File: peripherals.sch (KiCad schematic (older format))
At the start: 31 parts, among them J1 Conn_SWD, M1 Vibrator, Q1 NTR5103N, SW1 Btn_Up, SW2 Btn_Down, SW3 Btn_Select, SW4 Btn_Back, U1 ATSAMD21J18A-MU

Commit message: Finish up the schematic
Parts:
- removed C1, C3, C4, C5: 0.1uF, Capacitor_SMD:C_0603_1608Metric, symbol Device:C_Small
- removed C2: 4.7uF, Capacitor_SMD:C_0603_1608Metric, symbol Device:C_Small
- removed C6: 1uF, Capacitor_SMD:C_0603_1608Metric, symbol Device:C_Small
- removed D1: LED_TopLeft, LED_SMD_Extra:LED_RGBA_0606, symbol Device_Extra:LED_RGBA
- removed D2: LED_TopRight, LED_SMD_Extra:LED_RGBA_0606, symbol Device_Extra:LED_RGBA
- removed D3: LED_BottomLeft, LED_SMD_Extra:LED_RGBA_0606, symbol Device_Extra:LED_RGBA
- removed D4: LED_BottomRight, LED_SMD_Extra:LED_RGBA_0606, symbol Device_Extra:LED_RGBA
- removed J1: Conn_SWD, Connector_JST:JST_SH_SM04B-SRSS-TB_1x04-1MP_P1.00mm_Horizontal, symbol Connector_Generic:Conn_01x04
- removed M1: Vibrator, Buzzer_Beeper_Extra:C1026B, symbol Motor:Motor_DC
- removed Q1: NTR5103N, Package_TO_SOT_SMD:SOT-23, symbol Transistor_FET:BSS138
- removed R1: 1K, Resistor_SMD:R_0603_1608Metric, symbol Device:R_Small
- removed R10, R11, R12, R13, R2, R3, R4, R5, R6, R7, R8, R9: 360R, Resistor_SMD:R_0603_1608Metric, symbol Device:R_Small
- removed SW1: Btn_Up, Button_Switch_SMD_Extra:KLS7-TS2402, symbol Switch:SW_Push
- removed SW2: Btn_Down, Button_Switch_SMD_Extra:KLS7-TS2402, symbol Switch:SW_Push
- removed SW3: Btn_Select, Button_Switch_SMD_Extra:KLS7-TS2402, symbol Switch:SW_Push
- removed SW4: Btn_Back, Button_Switch_SMD_Extra:KLS7-TS2402, symbol Switch:SW_Push
- removed U1: ATSAMD21J18A-MU, Package_DFN_QFN:QFN-64-1EP_9x9mm_P0.5mm_EP4.7x4.7mm, symbol MCU_Microchip_SAMD:ATSAMD21J18A-MU
- added ANT1: ACAG1204-433-T, RF_Antenna_Extra:ACAG1204, symbol Device:Antenna
- added C10, C11, C12, C13, C14, C15, C9: 0.1uF, Capacitor_SMD:C_0603_1608Metric, symbol Device:C_Small
- added LS1: Speaker, symbol Device:Speaker
- added MK1: SPH0641LM4H, Sensor_Audio_Extra:SPH0641LM4H, symbol Sensor_Audio_Extra:SPH0641LM4H
- added R14, R15: 10K, Resistor_SMD:R_0603_1608Metric, symbol Device:R_Small
- added R16: 17K, Resistor_SMD:R_0603_1608Metric, symbol Device:R_Small
- added U3: LIS3DH, Package_LGA:LGA-16_3x3mm_P0.5mm_LayoutBorder3x5y, symbol Sensor_Motion_Extra:LIS3DH
- added U4: LPH7366, Display_Extra:Nokia_5110-3310_LCD, symbol Display_Graphic_Extra:LPH7366
- added U5: 26VF0168IS2AE, Package_SO:SOIJ-8_5.3x5.3mm_P1.27mm, symbol Memory_Flash_Extra:26VF0168IS2AE
- added U6: RFM69HCW, RF_Module:HOPERF_RFM69HW, symbol RF_AM_FM_Extra:RFM69HCW
- added U7: PAM8301, Package_TO_SOT_SMD:SOT-23-6, symbol Amplifier_Audio_Extra:PAM8301
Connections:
- net labels removed: +1V2, BTN_BACK, BTN_DOWN, BTN_SELECT, BTN_UP, LED1_B, LED1_G, LED1_R, LED2_B, LED2_G, LED2_R, LED3_B, LED3_G, LED3_R, LED4_B, LED4_G, LED4_R, SWDCLK, SWDIO, USB_D+, USB_D-, VIBRATOR
- wire segments 154 -> 93
- no-connect marks 1 -> 7
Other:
- note added: "433MHz Transceiver"
- note added: "Accelerometer"
- note added: "Display"
- note added: "Microphone"
- note added: "SPI Flash"
- note added: "Speaker"
- note removed: "I2SD1"
- note removed: "I2SSCK"
- note removed: "SERCOM0 - Display\nSERCOM1 - Accelerometer\nSERCOM3 - Flash\nSERCOM4 - RFM"
- note removed: "SERCOM0.0"
- note removed: "SERCOM0.1"
- note removed: "SERCOM1.0"
- note removed: "SERCOM1.1"
- note removed: "SERCOM3.0"
- note removed: "SERCOM3.2\n"
- note removed: "SERCOM3.3"
- note removed: "SERCOM4.0\n"
- note removed: "SERCOM4.1"
- note removed: "SERCOM4.2"
- note removed: "TCC"
- note removed: "VOUT0"

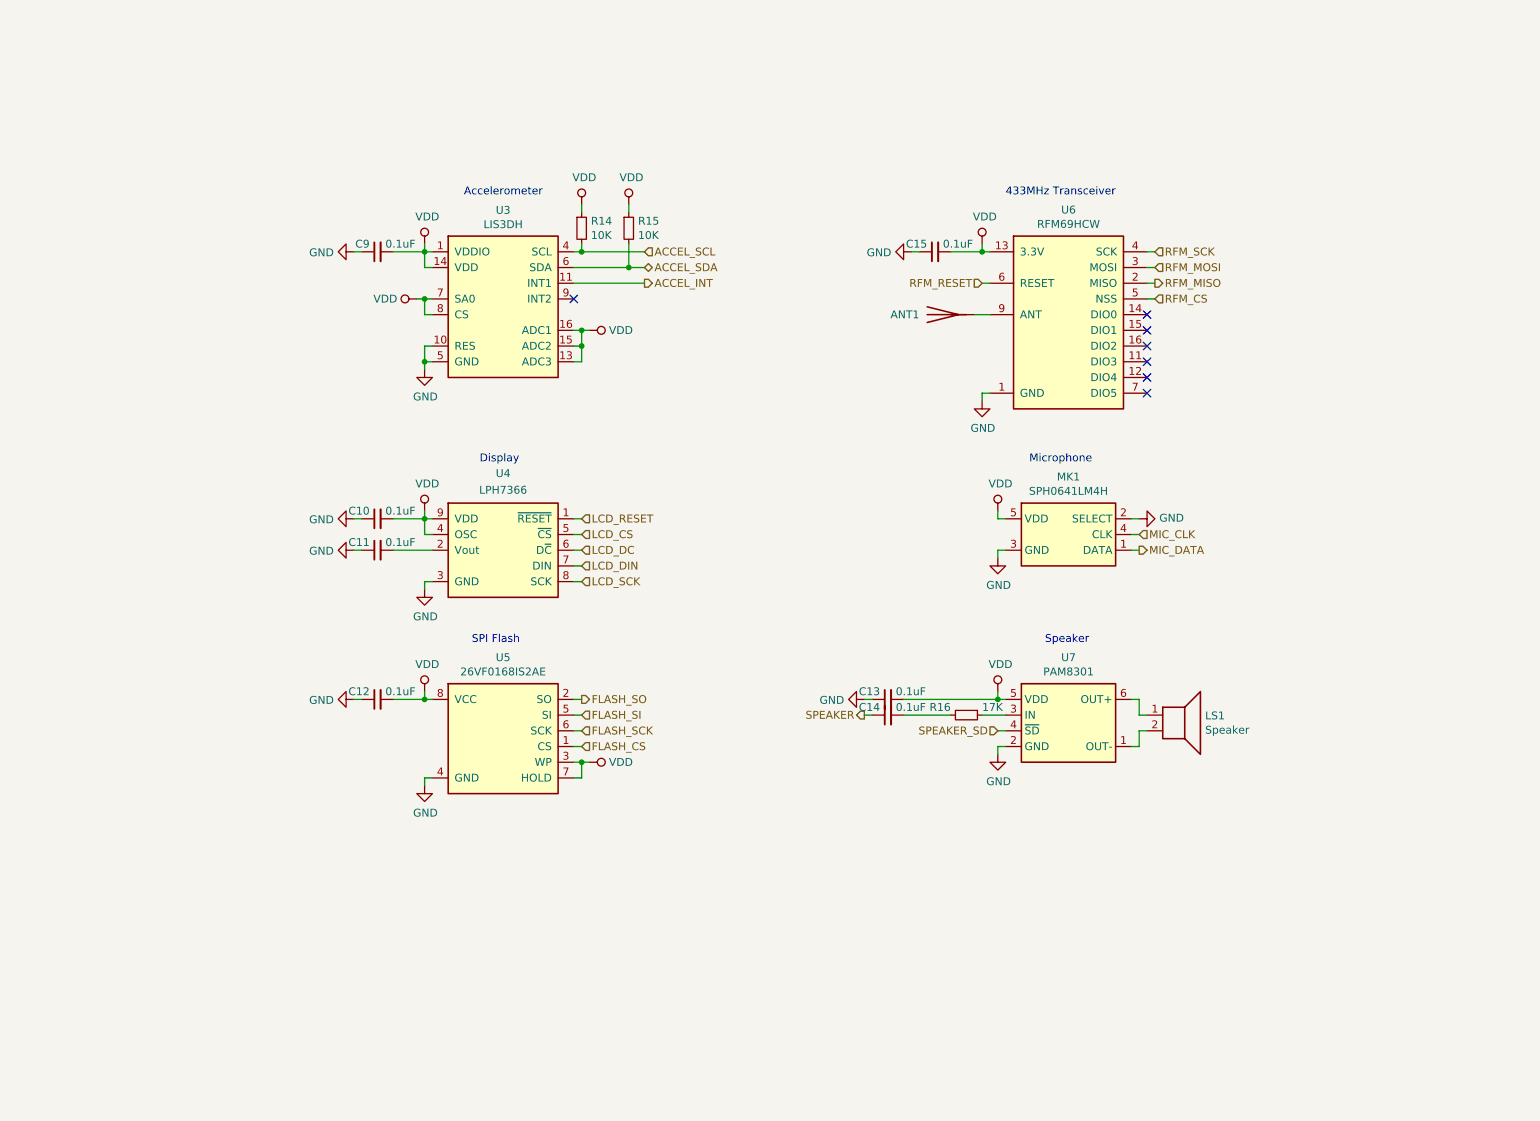
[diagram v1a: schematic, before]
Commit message: Change of plans, now a nRF52840 with E-ink
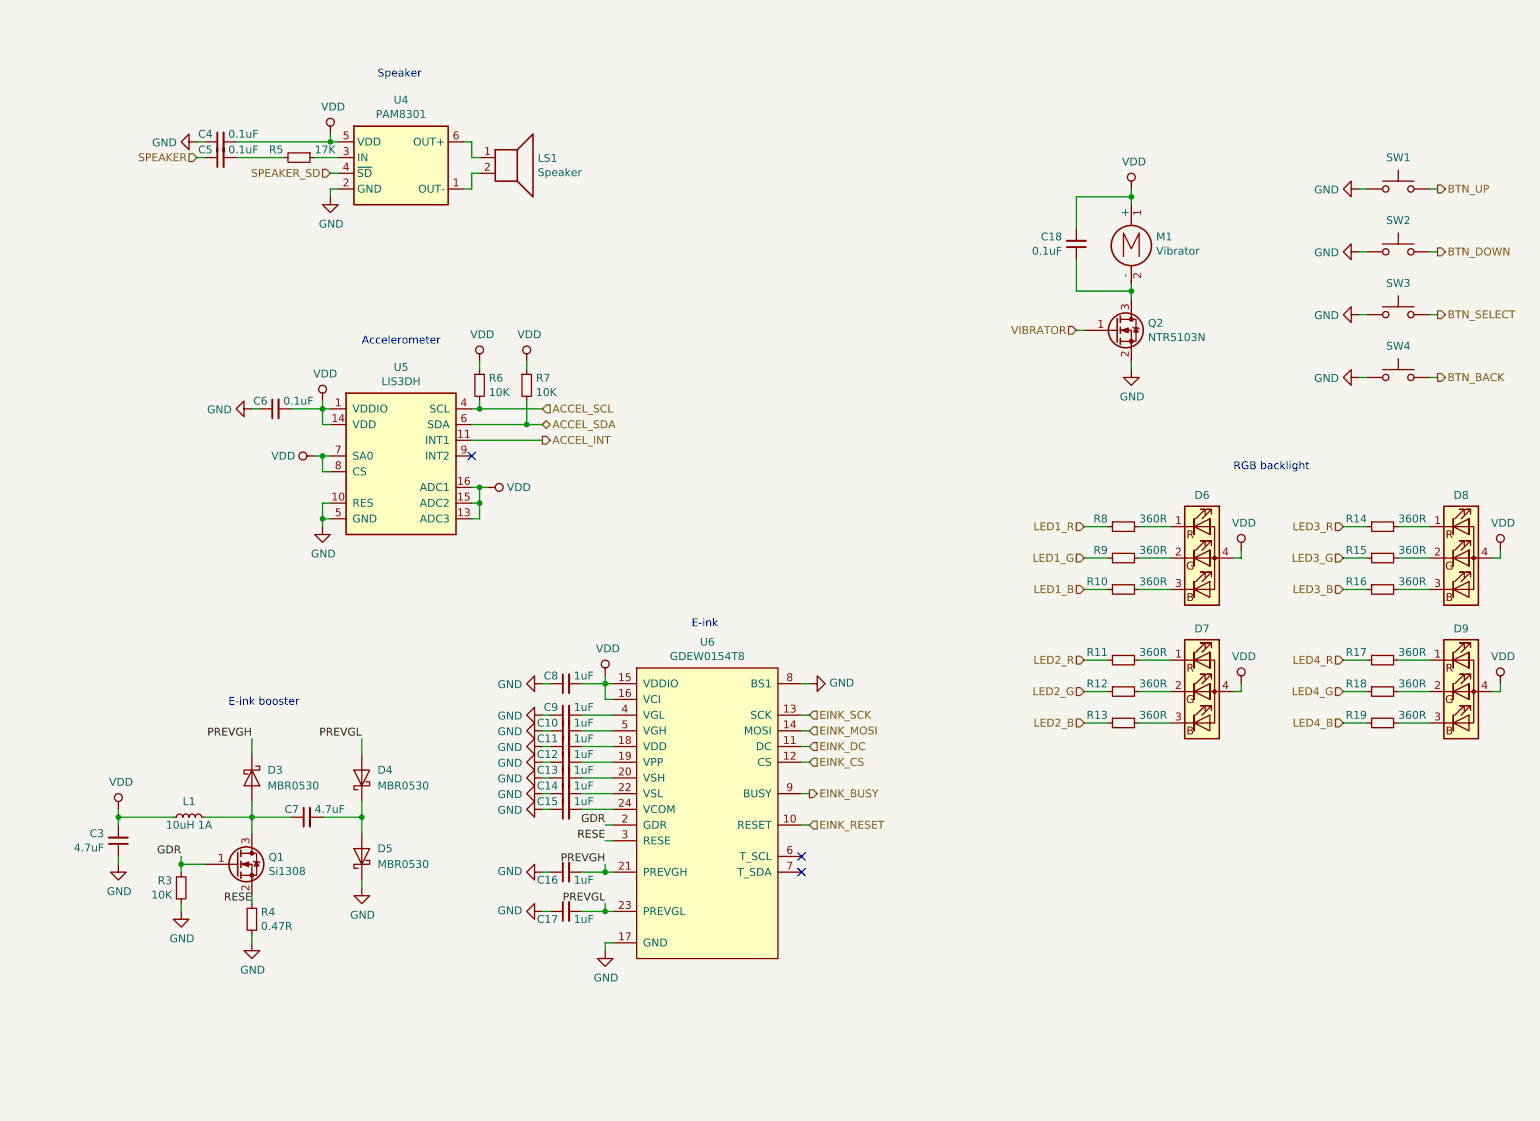
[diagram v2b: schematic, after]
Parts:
- removed ANT1: ACAG1204-433-T, RF_Antenna_Extra:ACAG1204, symbol Device:Antenna
- removed MK1: SPH0641LM4H, Sensor_Audio_Extra:SPH0641LM4H, symbol Sensor_Audio_Extra:SPH0641LM4H
- removed U3: LIS3DH, Package_LGA:LGA-16_3x3mm_P0.5mm_LayoutBorder3x5y, symbol Sensor_Motion_Extra:LIS3DH
- removed U4: LPH7366, Display_Extra:Nokia_5110-3310_LCD, symbol Display_Graphic_Extra:LPH7366
- removed U5: 26VF0168IS2AE, Package_SO:SOIJ-8_5.3x5.3mm_P1.27mm, symbol Memory_Flash_Extra:26VF0168IS2AE
- removed U6: RFM69HCW, RF_Module:HOPERF_RFM69HW, symbol RF_AM_FM_Extra:RFM69HCW
- removed U7: PAM8301, Package_TO_SOT_SMD:SOT-23-6, symbol Amplifier_Audio_Extra:PAM8301
- added C16, C17, C8: 1uF, Capacitor_SMD:C_0603_1608Metric, symbol Device:C_Small
- added C18, C4, C5, C6: 0.1uF, Capacitor_SMD:C_0603_1608Metric, symbol Device:C_Small
- added C3, C7: 4.7uF, Capacitor_SMD:C_0603_1608Metric, symbol Device:C_Small
- added D3, D4, D5: MBR0530, Diode_SMD:D_SOD-123, symbol Diode:MBR0530
- added D6: LED_TopLeft, LED_SMD_Extra:LED_RGBA_0606, symbol Device_Extra:LED_RGBA
- added D7: LED_TopRight, LED_SMD_Extra:LED_RGBA_0606, symbol Device_Extra:LED_RGBA
- added D8: LED_BottomLeft, LED_SMD_Extra:LED_RGBA_0606, symbol Device_Extra:LED_RGBA
- added D9: LED_BottomRight, LED_SMD_Extra:LED_RGBA_0606, symbol Device_Extra:LED_RGBA
- added L1: 10uH 1A, Inductor_SMD:L_Taiyo-Yuden_NR-60xx_HandSoldering, symbol Device:L_Small
- added M1: Vibrator, Buzzer_Beeper_Extra:C1026B, symbol Motor:Motor_DC
- added Q1: Si1308, Package_TO_SOT_SMD:SOT-23, symbol Transistor_FET:BSS138
- added Q2: NTR5103N, Package_TO_SOT_SMD:SOT-23, symbol Transistor_FET:BSS138
- added R10, R11, R12, R13, R17, R18, R19, R8, R9: 360R, Resistor_SMD:R_0603_1608Metric, symbol Device:R_Small
- added R3, R6, R7: 10K, Resistor_SMD:R_0603_1608Metric, symbol Device:R_Small
- added R4: 0.47R, Resistor_SMD:R_0603_1608Metric, symbol Device:R_Small
- added R5: 17K, Resistor_SMD:R_0603_1608Metric, symbol Device:R_Small
- added SW1: Btn_Up, Button_Switch_SMD_Extra:KLS7-TS2402, symbol Switch:SW_Push
- added SW2: Btn_Down, Button_Switch_SMD_Extra:KLS7-TS2402, symbol Switch:SW_Push
- added SW3: Btn_Select, Button_Switch_SMD_Extra:KLS7-TS2402, symbol Switch:SW_Push
- added SW4: Btn_Back, Button_Switch_SMD_Extra:KLS7-TS2402, symbol Switch:SW_Push
- added U4: PAM8301, Package_TO_SOT_SMD:SOT-23-6, symbol Amplifier_Audio_Extra:PAM8301
- added U5: LIS3DH, Package_LGA:LGA-16_3x3mm_P0.5mm_LayoutBorder3x5y, symbol Sensor_Motion_Extra:LIS3DH
- added U6: GDEW0154T8, symbol Display_Graphic_Extra:GDEW0154T8
- C10, C11, C12, C13, C14, C15, C9: value 0.1uF -> 1uF
- LS1: footprint (none) -> Symbol:CE-Logo_8.5x6mm_SilkScreen
- R14, R15: value 10K -> 360R
- R16: value 17K -> 360R
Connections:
- net ACCEL_INT: now also U5.11 (INT1)
- net ACCEL_SCL: now also R6.2, U5.4 (SCL); no longer R14.2
- net ACCEL_SDA: now also R7.2, U5.6 (SDA); no longer R15.2
- net GND: now also C14.1, C16.1, C17.1, C3.1, C4.1, C6.1, C8.1, D5.1 (K), Q2.2 (S), R3.1, R4.1, SW1.1, SW2.1, SW3.1, SW4.1, U4.2 (GND), U5.10 (RES), U5.12 (GND), U5.5 (GND), U6.17 (GND), U6.8 (BS1)
- net SPEAKER: now also C5.1; no longer C14.1
- net SPEAKER_SD: now also U4.4 (~SD)
- net VDD: now also C18.2, C3.2, C4.2, C6.2, C8.2, D6.4 (A), D7.4 (A), D8.4 (A), D9.4 (A), L1.2, M1.1 (+), R6.1, R7.1, U4.5 (VDD), U5.1 (VDDIO), U5.13 (ADC3), U5.14 (VDD), U5.15 (ADC2), U5.16 (ADC1), U5.7 (SA0), U5.8 (CS), U6.15 (VDDIO), U6.16 (VCI); no longer C10.2, C12.2, C13.2, C15.2, C9.2, R14.1, R15.1
- net at LS1.1: now also U4.6 (OUT+)
- net at LS1.2: now also U4.1 (OUT-)
- net LED3_B: now reaches R16.1
- net at C14.2: now also U6.22 (VSL); no longer R16.2
- net at C11.2: now also U6.18 (VDD)
- new net: R5.1, U4.3 (IN)
- new net: C5.2, R5.2
- new net: C12.2, U6.19 (VPP)
- new net: C13.2, U6.20 (VSH)
- new net: C15.2, U6.24 (VCOM)
- new net: C9.2, U6.4 (VGL)
- new net: C10.2, U6.5 (VGH)
- new net: C7.1, D3.2 (A), L1.1, Q1.3 (D)
- new net: C7.2, D4.1 (K), D5.2 (A)
- new net: D9.3 (BK), R19.2
- new net: D9.2 (GK), R18.2
- new net: D9.1 (RK), R17.2
- new net: D8.3 (BK), R16.2
- new net: D8.2 (GK), R15.2
- new net: D8.1 (RK), R14.2
- new net: D7.3 (BK), R13.2
- new net: D7.2 (GK), R12.2
- new net: D7.1 (RK), R11.2
- new net: D6.3 (BK), R10.2
- new net: D6.2 (GK), R9.2
- new net: D6.1 (RK), R8.2
- new net: C18.1, M1.2 (-), Q2.3 (D)
- new net BTN_BACK: SW4.2
- new net BTN_DOWN: SW2.2
- new net BTN_SELECT: SW3.2
- new net BTN_UP: SW1.2
- new net EINK_BUSY: U6.9 (BUSY)
- new net EINK_CS: U6.12 (CS)
- new net EINK_DC: U6.11 (DC)
- new net EINK_MOSI: U6.14 (MOSI)
- new net EINK_RESET: U6.10 (RESET)
- new net EINK_SCK: U6.13 (SCK)
- new net GDR: Q1.1 (G), R3.2, U6.2 (GDR)
- new net LED1_B: R10.1
- new net LED1_G: R9.1
- new net LED1_R: R8.1
- new net LED2_B: R13.1
- new net LED2_G: R12.1
- new net LED2_R: R11.1
- new net LED3_G: R15.1
- new net LED3_R: R14.1
- new net LED4_B: R19.1
- new net LED4_G: R18.1
- new net LED4_R: R17.1
- new net PREVGH: C16.2, D3.1 (K), U6.21 (PREVGH)
- new net PREVGL: C17.2, D4.2 (A), U6.23 (PREVGL)
- new net RESE: Q1.2 (S), R4.2, U6.3 (RESE)
- new net VIBRATOR: Q2.1 (G)
- no-connect marks 7 -> 3
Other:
- note added: "E-ink"
- note added: "E-ink booster"
- note added: "RGB backlight"
- note removed: "433MHz Transceiver"
- note removed: "Display"
- note removed: "Microphone"
- note removed: "SPI Flash"

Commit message: Finish rev1
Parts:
- L1: footprint Inductor_SMD:L_Taiyo-Yuden_NR-60xx_HandSoldering -> Inductor_SMD:L_Taiyo-Yuden_MD-3030; Part NRS6012T100 -> AISC-1210HS-100K-T2
- LS1: value Speaker -> CMT-5023S-SMT; footprint Symbol:CE-Logo_8.5x6mm_SilkScreen -> Buzzer_Beeper_Extra:CMT-5023S
- U6: footprint (none) -> Connector_GoodDisplay:GoodDisplay_24P-0.5SH_1x24-Horizontal
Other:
- note added: "Addr: 0x19"
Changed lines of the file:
@@
 AR Path="/5D0C1A3E" Ref="LS?"  Part="1"
 AR Path="/5D09C829/5D0C1A3E" Ref="LS1"  Part="1"
-F 0 "LS1" H 4220 1596 50  0000 L CNN
-F 1 "Speaker" H 4220 1505 50  0000 L CNN
-F 2 "Symbol:CE-Logo_8.5x6mm_SilkScreen" H 4050 1400 50  0001 C CNN
-F 3 "~" H 4040 1550 50  0001 C CNN
+F 0 "LS1" H 3950 1350 50  0000 L CNN
+F 1 "CMT-5023S-SMT" H 4220 1505 50  0001 L CNN
+F 2 "Buzzer_Beeper_Extra:CMT-5023S" H 4050 1400 50  0001 C CNN
+F 3 "https://www2.mouser.com/datasheet/2/670/cmt-5023s-smt-1310092.pdf" H 4040 1550 50  0001 C CNN
 	1    4050 1600
 	1    0    0    -1
@@
 F 0 "U6" H 5300 7015 50  0000 C CNN
 F 1 "GDEW0154T8" H 5300 6924 50  0000 C CNN
-F 2 "" H 5450 5500 50  0001 C CNN
+F 2 "Connector_GoodDisplay:GoodDisplay_24P-0.5SH_1x24-Horizontal" H 5450 5500 50  0001 C CNN
 F 3 "" H 5450 5500 50  0001 C CNN
 	1    5300 5850
@@
 F 0 "L1" V 2100 5800 50  0000 C CNN
 F 1 "10uH 1A" V 1950 5800 50  0000 C CNN
-F 2 "Inductor_SMD:L_Taiyo-Yuden_NR-60xx_HandSoldering" H 2000 5800 50  0001 C CNN
-F 3 "https://www2.mouser.com/datasheet/2/396/wound04_e-1290968.pdf" H 2000 5800 50  0001 C CNN
-F 4 "NRS6012T100" V 2000 5800 50  0001 C CNN "Part"
+F 2 "Inductor_SMD:L_Taiyo-Yuden_MD-3030" H 2000 5800 50  0001 C CNN
+F 3 "https://www2.mouser.com/datasheet/2/3/AISC-1210HS-14392.pdf" H 2000 5800 50  0001 C CNN
+F 4 "AISC-1210HS-100K-T2" V 2000 5800 50  0001 C CNN "Part"
 	1    2000 5800
 	0    1    -1   0
@@
 EndData
 $EndBitmap
+Text Notes 3150 4100 0    50   ~ 0
+Addr: 0x19
 $EndSCHEMATC
